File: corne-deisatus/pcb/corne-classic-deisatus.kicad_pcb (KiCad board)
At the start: 2 copper layers, 149.4 x 94.7 mm, 101 parts, among them J1 MJ-4PP-9, J2 OLED, J3 LED, P1 i2c-pin, P2 i2c-pin, SW1 SW_PUSH, SW10 SW_PUSH, SW11 SW_PUSH, SW12 SW_PUSH, SW13 SW_PUSH, SW14 SW_PUSH, SW15 SW_PUSH, SW16 SW_PUSH, SW17 SW_PUSH, SW18 SW_PUSH, SW19 SW_PUSH, SW2 SW_PUSH, SW20 SW_PUSH, SW21 SW_PUSH, SW22 SW_PUSH, SW3 SW_PUSH, SW4 SW_PUSH, SW5 SW_PUSH, SW6 SW_PUSH, SW7 SW_PUSH, SW8 SW_PUSH, SW9 SW_PUSH, U1 ProMicro

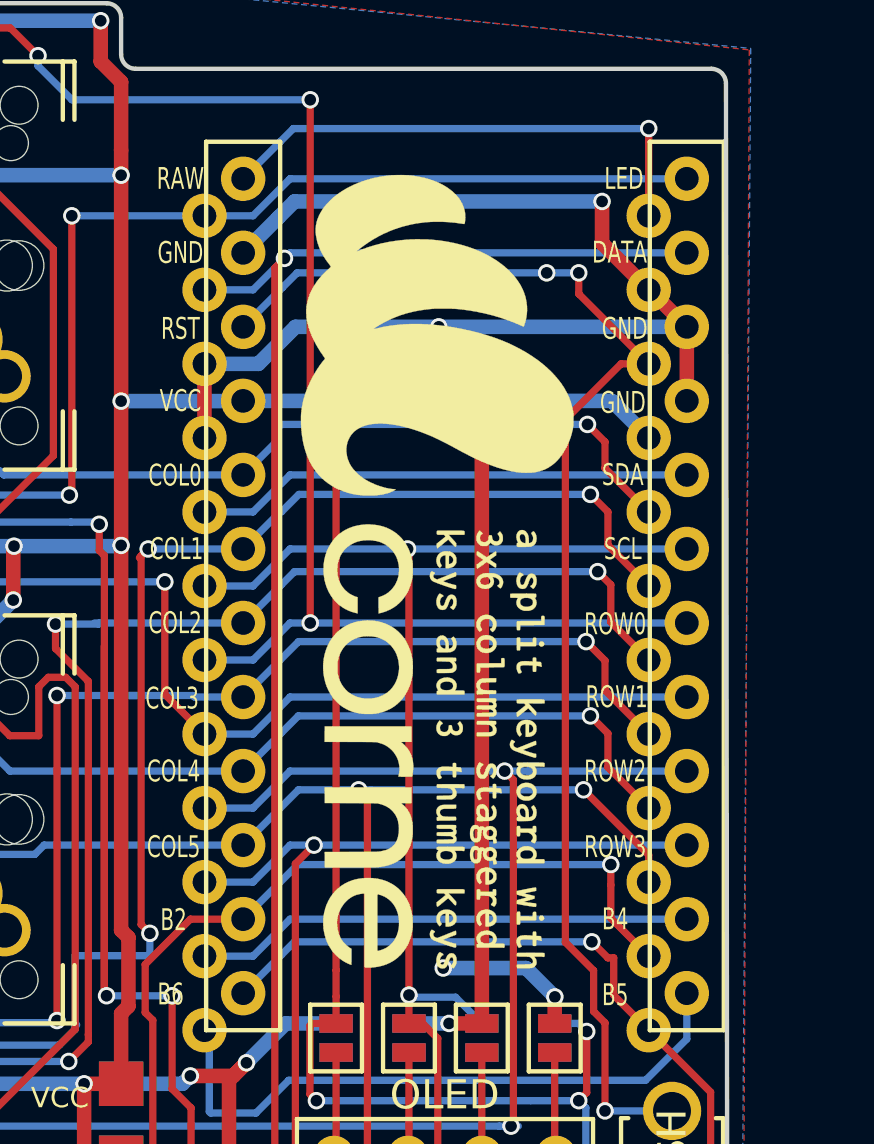
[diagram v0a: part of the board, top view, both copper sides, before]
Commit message: rebuilt gerbers, changed file names
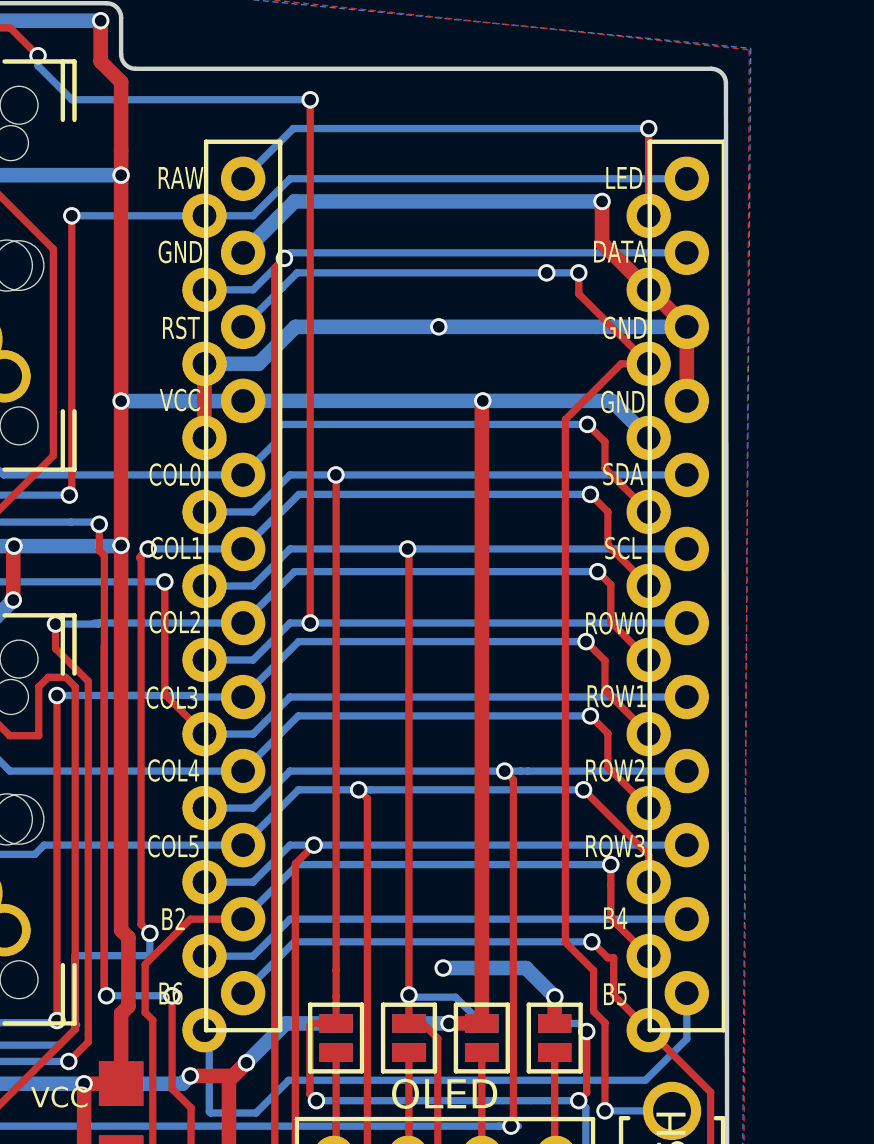
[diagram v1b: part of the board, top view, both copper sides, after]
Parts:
- removed G*** (x2): LOGO, kbd:corne
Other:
- board text added: "Corne Classic v2.0 PCB designed by foostan Modified by Arina57"
- board text removed: "Corne Classic v2.0 PCB designed by foostan"

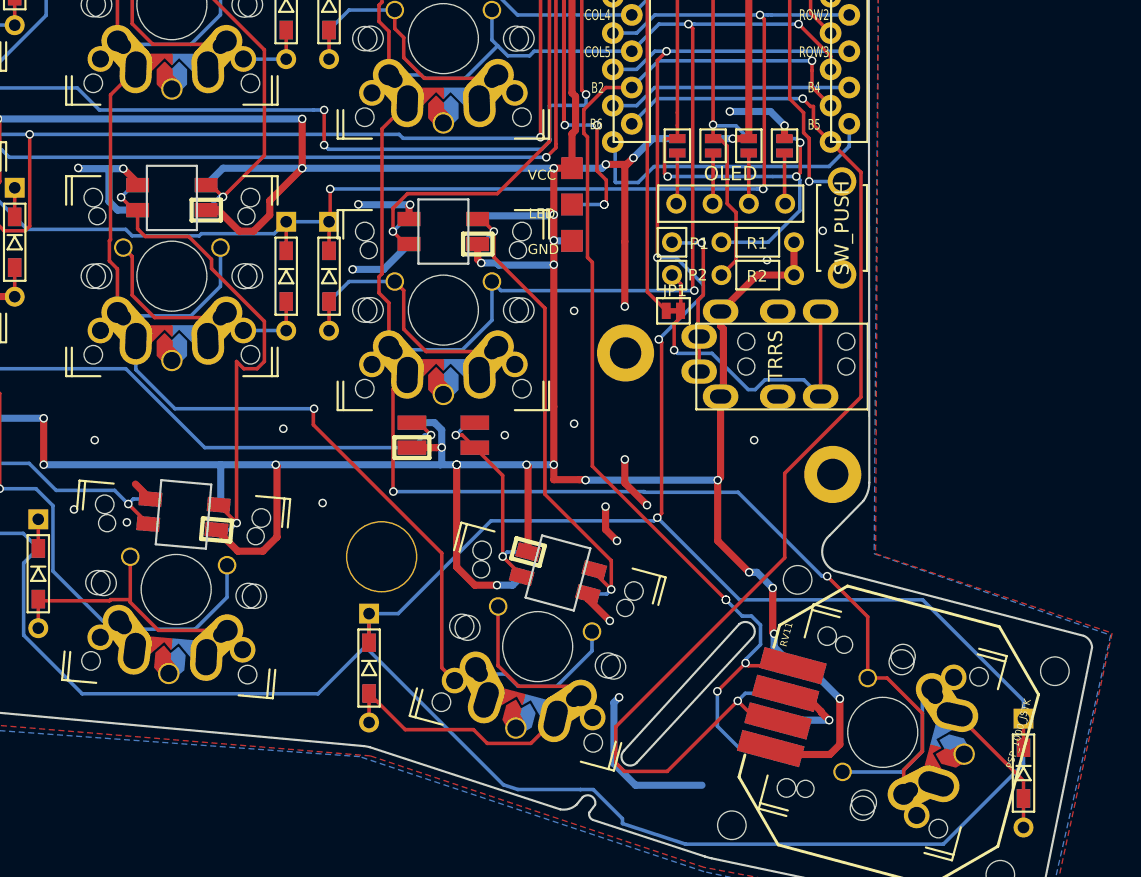
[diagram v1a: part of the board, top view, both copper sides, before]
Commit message: Updated PCB for new pins
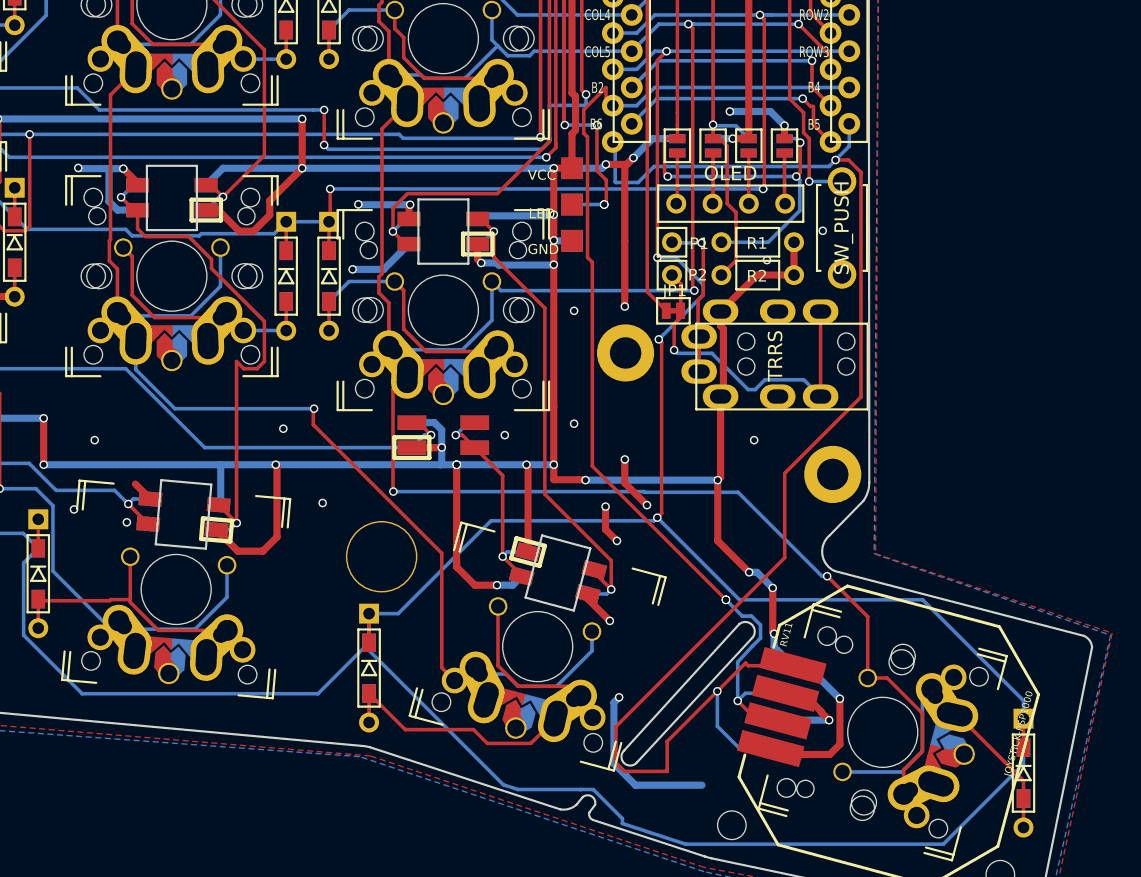
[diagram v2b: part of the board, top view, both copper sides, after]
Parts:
- RV11: value PSP_1000_JSTK -> JOYSTICK-PSP1000; footprint HackPack_Footprints:JOYSTICK-PSP1000-reverse -> HackPack_Footprints:JOYSTICK-PSP1000
- SW20, SW21: footprint kailh-pg1425-x-switch:MX-ALPS-Choc-X-straight-crane2-u1.5 -> kailh-pg1425-x-switch:MX-ALPS-Choc-X-straight-crane2
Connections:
- U1 pad 11: Net-(U1-Pad11) -> analogY
- U1 pad 12: Net-(U1-Pad12) -> analogX
- U1 pad 13: analogY -> Net-(U1-Pad13)
- U1 pad 14: analogX -> Net-(U1-Pad14)
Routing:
- net Net-(U1-Pad12): track 21.9 -> 0.00 mm
- net analogX: track 79.5 -> 97.0 mm, vias 5 -> 2
- net Net-(U1-Pad14): track 0.00 -> 17.2 mm, vias 0 -> 1
- net Net-(U1-Pad11): track 17.1 -> 0.00 mm
- net Net-(U1-Pad13): track 0.00 -> 16.7 mm, vias 0 -> 1
- net analogY: track 88.0 -> 77.4 mm, vias 2 -> 3
